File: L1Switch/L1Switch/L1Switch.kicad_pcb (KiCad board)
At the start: 4 copper layers, 119 parts, among them J1 RJSNEGF8A08, J2 Conn_01x07_Male, J3 Barrel_Jack, T1 SM51589PEL, T2 SM51589PEL, U1 XC7A15T-FTG256, U2 VSC8658, U3 TPS548A20RVE, U4 TPS565208, U5 TPS565208, U6 TPS565208

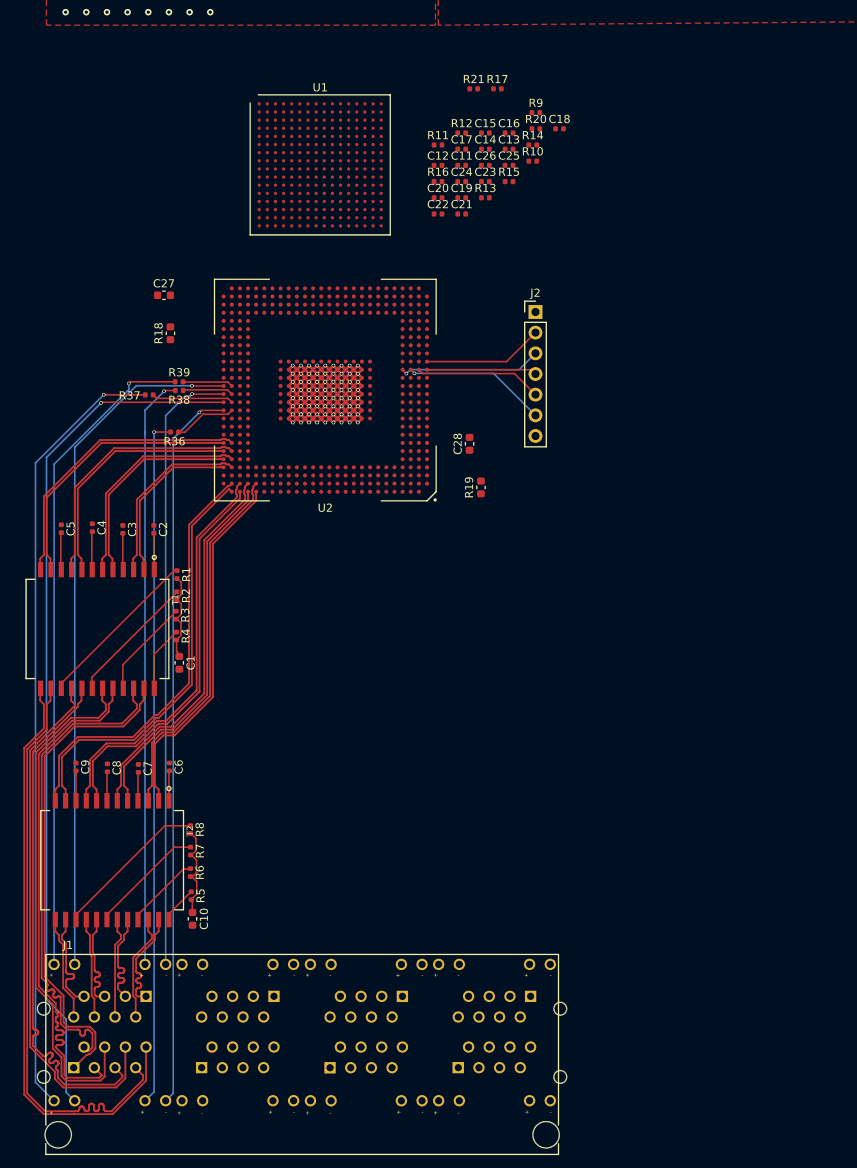
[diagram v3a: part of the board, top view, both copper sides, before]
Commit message: Connect/route 8 ports to PHY.
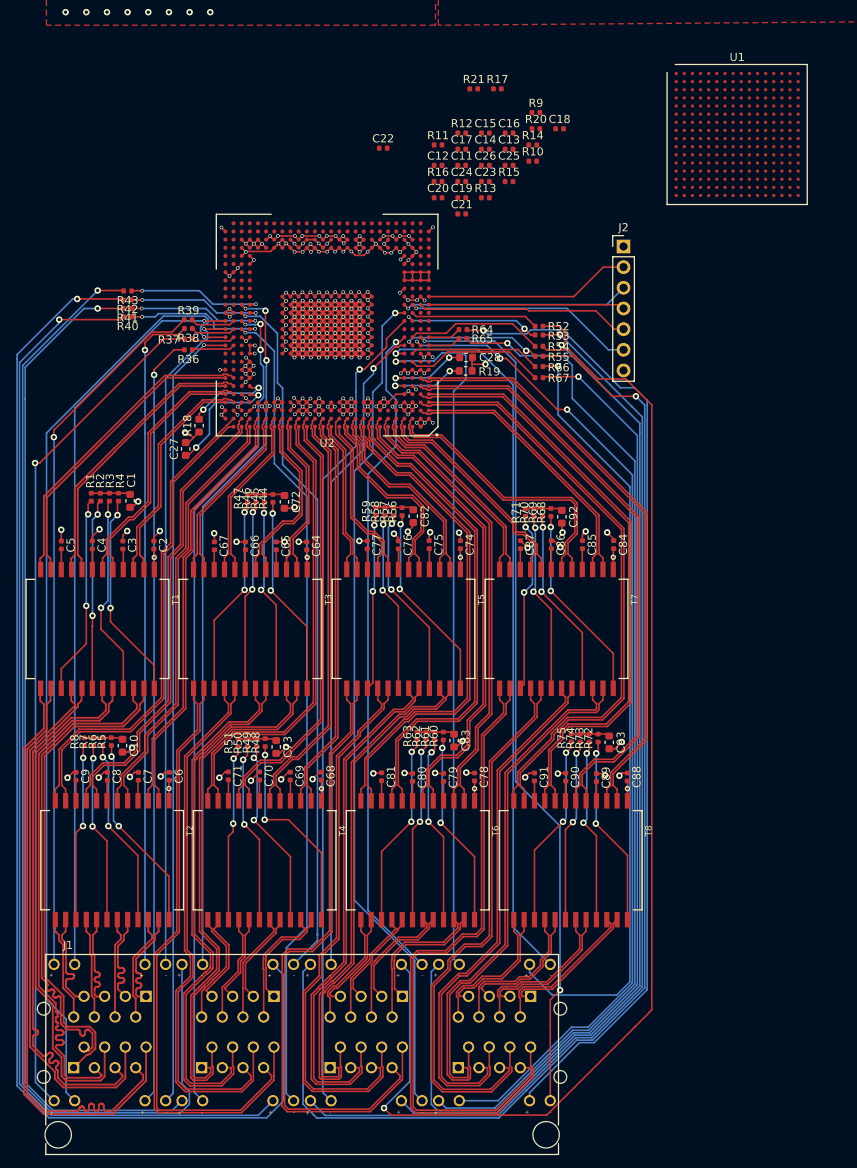
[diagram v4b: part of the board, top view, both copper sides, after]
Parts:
- added C64: 0.1 uF, Capacitor_SMD:C_0402_1005Metric, F.Cu at (104.8, 80.1)
- added C65: 0.1 uF, Capacitor_SMD:C_0402_1005Metric, F.Cu at (101.0, 80.1)
- added C66: 0.1 uF, Capacitor_SMD:C_0402_1005Metric, F.Cu at (97.2, 80.1)
- added C67: 0.1 uF, Capacitor_SMD:C_0402_1005Metric, F.Cu at (93.4, 80.1)
- added C68: 0.1 uF, Capacitor_SMD:C_0402_1005Metric, F.Cu at (106.6, 108.4)
- added C69: 0.1 uF, Capacitor_SMD:C_0402_1005Metric, F.Cu at (102.7, 108.4)
- added C70: 0.1 uF, Capacitor_SMD:C_0402_1005Metric, F.Cu at (99.0, 108.3)
- added C71: 0.1 uF, Capacitor_SMD:C_0402_1005Metric, F.Cu at (95.1, 108.3)
- added C72: 1000pF, 2KV, Capacitor_SMD:C_0603_1608Metric, F.Cu at (102.0, 74.7)
- added C73: 1000pF, 2KV, Capacitor_SMD:C_0603_1608Metric, F.Cu at (101.0, 104.8)
- added C74: 0.1 uF, Capacitor_SMD:C_0402_1005Metric, F.Cu at (123.7, 79.9)
- added C75: 0.1 uF, Capacitor_SMD:C_0402_1005Metric, F.Cu at (119.8, 79.9)
- added C76: 0.1 uF, Capacitor_SMD:C_0402_1005Metric, F.Cu at (116.0, 79.9)
- added C77: 0.1 uF, Capacitor_SMD:C_0402_1005Metric, F.Cu at (112.2, 79.9)
- added C78: 0.1 uF, Capacitor_SMD:C_0402_1005Metric, F.Cu at (125.4, 108.5)
- added C79: 0.1 uF, Capacitor_SMD:C_0402_1005Metric, F.Cu at (121.6, 108.5)
- added C80: 0.1 uF, Capacitor_SMD:C_0402_1005Metric, F.Cu at (117.8, 108.5)
- added C81: 0.1 uF, Capacitor_SMD:C_0402_1005Metric, F.Cu at (114.0, 108.4)
- added C82: 1000pF, 2KV, Capacitor_SMD:C_0603_1608Metric, F.Cu at (117.9, 76.4)
- added C83: 1000pF, 2KV, Capacitor_SMD:C_0603_1608Metric, F.Cu at (122.9, 104.0)
- added C84: 0.1 uF, Capacitor_SMD:C_0402_1005Metric, F.Cu at (142.5, 79.9)
- added C85: 0.1 uF, Capacitor_SMD:C_0402_1005Metric, F.Cu at (138.7, 79.9)
- added C86: 0.1 uF, Capacitor_SMD:C_0402_1005Metric, F.Cu at (134.8, 79.9)
- added C87: 0.1 uF, Capacitor_SMD:C_0402_1005Metric, F.Cu at (131.1, 79.9)
- added C88: 0.1 uF, Capacitor_SMD:C_0402_1005Metric, F.Cu at (144.2, 108.5)
- added C89: 0.1 uF, Capacitor_SMD:C_0402_1005Metric, F.Cu at (140.4, 108.5)
- added C90: 0.1 uF, Capacitor_SMD:C_0402_1005Metric, F.Cu at (136.6, 108.5)
- added C91: 0.1 uF, Capacitor_SMD:C_0402_1005Metric, F.Cu at (132.8, 108.5)
- added C92: 1000pF, 2KV, Capacitor_SMD:C_0603_1608Metric, F.Cu at (136.1, 76.5)
- added C93: 1000pF, 2KV, Capacitor_SMD:C_0603_1608Metric, F.Cu at (142.0, 104.2)
- added R40: 75R0, Resistor_SMD:R_0402_1005Metric, F.Cu at (82.8, 51.9)
- added R41: 75R0, Resistor_SMD:R_0402_1005Metric, F.Cu at (82.7, 50.9)
- added R42: 75R0, Resistor_SMD:R_0402_1005Metric, F.Cu at (82.7, 49.8)
- added R43: 75R0, Resistor_SMD:R_0402_1005Metric, F.Cu at (82.8, 48.7)
- added R44: 75R0, Resistor_SMD:R_0402_1005Metric, F.Cu at (100.6, 74.2)
- added R45: 75R0, Resistor_SMD:R_0402_1005Metric, F.Cu at (99.6, 74.2)
- added R46: 75R0, Resistor_SMD:R_0402_1005Metric, F.Cu at (98.5, 74.2)
- added R47: 75R0, Resistor_SMD:R_0402_1005Metric, F.Cu at (97.5, 74.2)
- added R48: 75R0, Resistor_SMD:R_0402_1005Metric, F.Cu at (99.7, 104.2)
- added R49: 75R0, Resistor_SMD:R_0402_1005Metric, F.Cu at (98.6, 104.2)
- added R50: 75R0, Resistor_SMD:R_0402_1005Metric, F.Cu at (97.5, 104.3)
- added R51: 75R0, Resistor_SMD:R_0402_1005Metric, F.Cu at (96.3, 104.3)
- added R52: 75R0, Resistor_SMD:R_0402_1005Metric, F.Cu at (133.3, 53.1)
- added R53: 75R0, Resistor_SMD:R_0402_1005Metric, F.Cu at (133.3, 54.1)
- added R54: 75R0, Resistor_SMD:R_0402_1005Metric, F.Cu at (133.3, 55.5)
- added R55: 75R0, Resistor_SMD:R_0402_1005Metric, F.Cu at (133.3, 56.7)
- added R56: 75R0, Resistor_SMD:R_0402_1005Metric, F.Cu at (116.5, 75.8)
- added R57: 75R0, Resistor_SMD:R_0402_1005Metric, F.Cu at (115.5, 75.8)
- added R58: 75R0, Resistor_SMD:R_0402_1005Metric, F.Cu at (114.4, 75.8)
- added R59: 75R0, Resistor_SMD:R_0402_1005Metric, F.Cu at (113.3, 75.8)
- added R60: 75R0, Resistor_SMD:R_0402_1005Metric, F.Cu at (121.6, 103.4)
- added R61: 75R0, Resistor_SMD:R_0402_1005Metric, F.Cu at (120.5, 103.4)
- added R62: 75R0, Resistor_SMD:R_0402_1005Metric, F.Cu at (119.4, 103.4)
- added R63: 75R0, Resistor_SMD:R_0402_1005Metric, F.Cu at (118.3, 103.4)
- added R64: 75R0, Resistor_SMD:R_0402_1005Metric, F.Cu at (124.0, 53.5)
- added R65: 75R0, Resistor_SMD:R_0402_1005Metric, F.Cu at (124.0, 54.6)
- added R66: 75R0, Resistor_SMD:R_0402_1005Metric, F.Cu at (133.3, 58.0)
- added R67: 75R0, Resistor_SMD:R_0402_1005Metric, F.Cu at (133.3, 59.4)
- added R68: 75R0, Resistor_SMD:R_0402_1005Metric, F.Cu at (134.8, 75.9)
- added R69: 75R0, Resistor_SMD:R_0402_1005Metric, F.Cu at (133.7, 75.9)
- added R70: 75R0, Resistor_SMD:R_0402_1005Metric, F.Cu at (132.7, 76.0)
- added R71: 75R0, Resistor_SMD:R_0402_1005Metric, F.Cu at (131.7, 75.9)
- added R72: 75R0, Resistor_SMD:R_0402_1005Metric, F.Cu at (140.6, 103.7)
- added R73: 75R0, Resistor_SMD:R_0402_1005Metric, F.Cu at (139.5, 103.7)
- added R74: 75R0, Resistor_SMD:R_0402_1005Metric, F.Cu at (138.4, 103.7)
- added R75: 75R0, Resistor_SMD:R_0402_1005Metric, F.Cu at (137.3, 103.7)
- added T3: SM51589PEL, L1Switch:SM51589PEL, F.Cu at (97.8, 90.3)
- added T4: SM51589PEL, L1Switch:SM51589PEL, F.Cu at (99.6, 118.7)
- added T5: SM51589PEL, L1Switch:SM51589PEL, F.Cu at (116.7, 90.3)
- added T6: SM51589PEL, L1Switch:SM51589PEL, F.Cu at (118.4, 118.7)
- added T7: SM51589PEL, L1Switch:SM51589PEL, F.Cu at (135.5, 90.3)
- added T8: SM51589PEL, L1Switch:SM51589PEL, F.Cu at (137.2, 118.7)
- moved U1 51.4 mm to (157.7, 29.5)
- moved C10 23.0 mm to (82.1, 104.6)
- moved R5 21.4 mm to (80.7, 104.1), turned to 90 degrees
- moved C1 20.8 mm to (83.1, 74.5)
- moved R6 19.4 mm to (79.7, 104.1), turned to 90 degrees
- moved C27 19.1 mm to (89.9, 68.1), turned to 90 degrees
- moved R4 18.5 mm to (81.6, 74.1), turned to 90 degrees
- moved R7 18.0 mm to (78.5, 104.1), turned to 90 degrees
- moved R8 16.9 mm to (77.4, 104.1), turned to 90 degrees
- moved R3 16.7 mm to (80.5, 74.1), turned to 90 degrees
- moved R2 15.3 mm to (79.4, 74.1), turned to 90 degrees
- moved R19 14.4 mm to (124.3, 58.5), turned to 180 degrees
- moved R1 14.2 mm to (78.3, 74.1), turned to 90 degrees
- moved J2 13.5 mm to (143.7, 43.3)
- moved R18 11.9 mm to (91.5, 65.3)
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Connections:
- J1 pad 31: Net-(J1-Pad31) -> /Net 1/P3.A+
- J1 pad 311: Net-(J1-Pad311) -> /Net 1/P3.LED2
- J1 pad 32: Net-(J1-Pad32) -> /Net 1/P3.A-
- J1 pad 33: Net-(J1-Pad33) -> /Net 1/P3.B+
- J1 pad 34: Net-(J1-Pad34) -> /Net 1/P3.B-
- J1 pad 35: Net-(J1-Pad35) -> /Net 1/P3.C+
- J1 pad 36: Net-(J1-Pad36) -> /Net 1/P3.C-
- J1 pad 37: Net-(J1-Pad37) -> /Net 1/P3.D+
- J1 pad 38: Net-(J1-Pad38) -> /Net 1/P3.D-
- J1 pad 39: Net-(J1-Pad39) -> /Net 1/P3.LED0
- J1 pad 41: Net-(J1-Pad41) -> /Net 1/P4.A+
- J1 pad 411: Net-(J1-Pad411) -> /Net 1/P4.LED2
- J1 pad 42: Net-(J1-Pad42) -> /Net 1/P4.A-
- J1 pad 43: Net-(J1-Pad43) -> /Net 1/P4.B+
- J1 pad 44: Net-(J1-Pad44) -> /Net 1/P4.B-
- J1 pad 45: Net-(J1-Pad45) -> /Net 1/P4.C+
- J1 pad 46: Net-(J1-Pad46) -> /Net 1/P4.C-
- J1 pad 47: Net-(J1-Pad47) -> /Net 1/P4.D+
- J1 pad 48: Net-(J1-Pad48) -> /Net 1/P4.D-
- J1 pad 49: Net-(J1-Pad49) -> /Net 1/P4.LED0
- J1 pad 51: Net-(J1-Pad51) -> /Net 1/P5.A+
- J1 pad 511: Net-(J1-Pad511) -> /Net 1/P5.LED2
- J1 pad 52: Net-(J1-Pad52) -> /Net 1/P5.A-
- J1 pad 53: Net-(J1-Pad53) -> /Net 1/P5.B+
- J1 pad 54: Net-(J1-Pad54) -> /Net 1/P5.B-
- J1 pad 55: Net-(J1-Pad55) -> /Net 1/P5.C+
- J1 pad 56: Net-(J1-Pad56) -> /Net 1/P5.C-
- J1 pad 57: Net-(J1-Pad57) -> /Net 1/P5.D+
- J1 pad 58: Net-(J1-Pad58) -> /Net 1/P5.D-
- J1 pad 59: Net-(J1-Pad59) -> /Net 1/P5.LED0
- J1 pad 61: Net-(J1-Pad61) -> /Net 1/P6.A+
- J1 pad 611: Net-(J1-Pad611) -> /Net 1/P6.LED2
- J1 pad 62: Net-(J1-Pad62) -> /Net 1/P6.A-
- J1 pad 63: Net-(J1-Pad63) -> /Net 1/P6.B+
- J1 pad 64: Net-(J1-Pad64) -> /Net 1/P6.B-
- J1 pad 65: Net-(J1-Pad65) -> /Net 1/P6.C+
- J1 pad 66: Net-(J1-Pad66) -> /Net 1/P6.C-
- J1 pad 67: Net-(J1-Pad67) -> /Net 1/P6.D+
- J1 pad 68: Net-(J1-Pad68) -> /Net 1/P6.D-
- J1 pad 69: Net-(J1-Pad69) -> /Net 1/P6.LED0
- J1 pad 71: Net-(J1-Pad71) -> /Net 1/P7.A+
- J1 pad 711: Net-(J1-Pad711) -> /Net 1/P7.LED2
- J1 pad 72: Net-(J1-Pad72) -> /Net 1/P7.A-
- J1 pad 73: Net-(J1-Pad73) -> /Net 1/P7.B+
- J1 pad 74: Net-(J1-Pad74) -> /Net 1/P7.B-
- J1 pad 75: Net-(J1-Pad75) -> /Net 1/P7.C+
- J1 pad 76: Net-(J1-Pad76) -> /Net 1/P7.C-
- J1 pad 77: Net-(J1-Pad77) -> /Net 1/P7.D+
- J1 pad 78: Net-(J1-Pad78) -> /Net 1/P7.D-
- J1 pad 79: Net-(J1-Pad79) -> /Net 1/P7.LED0
- J1 pad 81: Net-(J1-Pad81) -> /Net 1/P8.A+
- J1 pad 811: Net-(J1-Pad811) -> /Net 1/P8.LED2
- J1 pad 82: Net-(J1-Pad82) -> /Net 1/P8.A-
- J1 pad 83: Net-(J1-Pad83) -> /Net 1/P8.B+
- J1 pad 84: Net-(J1-Pad84) -> /Net 1/P8.B-
- J1 pad 85: Net-(J1-Pad85) -> /Net 1/P8.C+
- J1 pad 86: Net-(J1-Pad86) -> /Net 1/P8.C-
- J1 pad 87: Net-(J1-Pad87) -> /Net 1/P8.D+
- J1 pad 88: Net-(J1-Pad88) -> /Net 1/P8.D-
- J1 pad 89: Net-(J1-Pad89) -> /Net 1/P8.LED0
- U2 pad J3: Net-(U2-PadJ3) -> /Net 1/P8.LED3
- U2 pad J4: Net-(U2-PadJ4) -> /Net 1/P8.LED2
- U2 pad K3: Net-(U2-PadK3) -> /Net 1/P8.LED1
- U2 pad K4: Net-(U2-PadK4) -> /Net 1/P8.LED0
- U2 pad L1: Net-(U2-PadL1) -> /Net 1/P7.LED3
- U2 pad L2: Net-(U2-PadL2) -> /Net 1/P7.LED2
- U2 pad L3: Net-(U2-PadL3) -> /Net 1/P6.LED3
- U2 pad L4: Net-(U2-PadL4) -> /Net 1/P6.LED2
- U2 pad M1: Net-(U2-PadM1) -> /Net 1/P7.LED1
- U2 pad M2: Net-(U2-PadM2) -> /Net 1/P7.LED0
- U2 pad M3: Net-(U2-PadM3) -> /Net 1/P6.LED1
- U2 pad M4: Net-(U2-PadM4) -> /Net 1/P6.LED0
- U2 pad N23: Net-(U2-PadN23) -> /Net 1/P3.LED1
- U2 pad N24: Net-(U2-PadN24) -> /Net 1/P3.LED0
- U2 pad P23: Net-(U2-PadP23) -> /Net 1/P3.LED3
- U2 pad P24: Net-(U2-PadP24) -> /Net 1/P3.LED2
- U2 pad P3: Net-(U2-PadP3) -> /Net 1/P5.LED3
- U2 pad P4: Net-(U2-PadP4) -> /Net 1/P5.LED2
- U2 pad R23: Net-(U2-PadR23) -> /Net 1/P4.LED1
- U2 pad R24: Net-(U2-PadR24) -> /Net 1/P4.LED0
- U2 pad R3: Net-(U2-PadR3) -> /Net 1/P5.LED1
- U2 pad R4: Net-(U2-PadR4) -> /Net 1/P5.LED0
- U2 pad T23: Net-(U2-PadT23) -> /Net 1/P4.LED3
- U2 pad T24: Net-(U2-PadT24) -> /Net 1/P4.LED2
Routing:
- net Net-(J1-Pad410): track 0.00 -> 158.4 mm, vias 0 -> 1
- net Net-(J1-Pad612): track 0.00 -> 153.5 mm, vias 0 -> 1
- net Net-(J1-Pad610): track 0.00 -> 148.8 mm, vias 0 -> 1
- net Net-(J1-Pad412): track 0.00 -> 144.5 mm, vias 0 -> 1
- net Net-(J1-Pad310): track 0.00 -> 137.5 mm, vias 0 -> 1
- net Net-(J1-Pad512): track 0.00 -> 134.7 mm, vias 0 -> 1
- net Net-(J1-Pad812): track 0.00 -> 131.8 mm, vias 0 -> 1
- net Net-(J1-Pad712): track 0.00 -> 124.4 mm, vias 0 -> 1
- net Net-(J1-Pad312): track 0.00 -> 124.2 mm, vias 0 -> 1
- net Net-(J1-Pad510): track 0.00 -> 123.9 mm, vias 0 -> 1
- net /Net 1/P7.LED2: track 0.00 -> 123.7 mm, vias 0 -> 3
- net Net-(J1-Pad710): track 0.00 -> 119.3 mm, vias 0 -> 1
- net GND: track 224.0 -> 333.4 mm, vias 135 -> 212
- net /Net 1/P7.LED0: track 0.00 -> 106.5 mm, vias 0 -> 2
- net /Net 1/P5.LED0: track 0.00 -> 103.5 mm, vias 0 -> 1
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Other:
- net class Default: clearance 0.127 -> 0.1; trace_width 0.2 -> 0.2032
- net class Diff_100: clearance 0.127 -> 0.1; trace_width 0.2286 -> 0.2032
- rule trace_clearance: 0.127 -> 0.1
